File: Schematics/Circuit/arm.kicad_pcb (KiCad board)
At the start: 2 copper layers, 15.1 x 13.2 mm, 6 parts, among them IC1 VL53L0X, J1 Conn_01x07

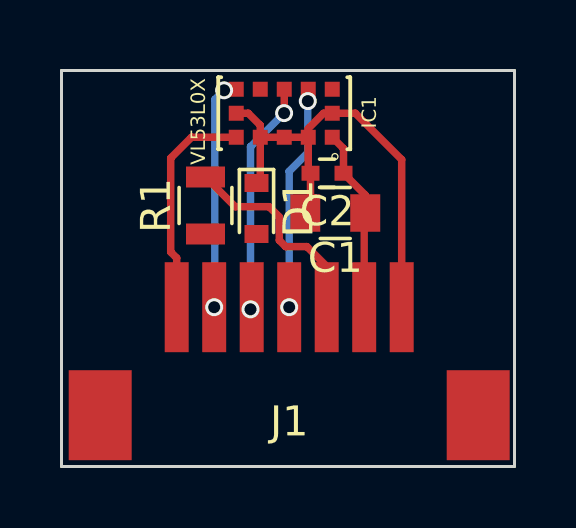
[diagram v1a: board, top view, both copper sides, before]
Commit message: Edit schematic and model, add images
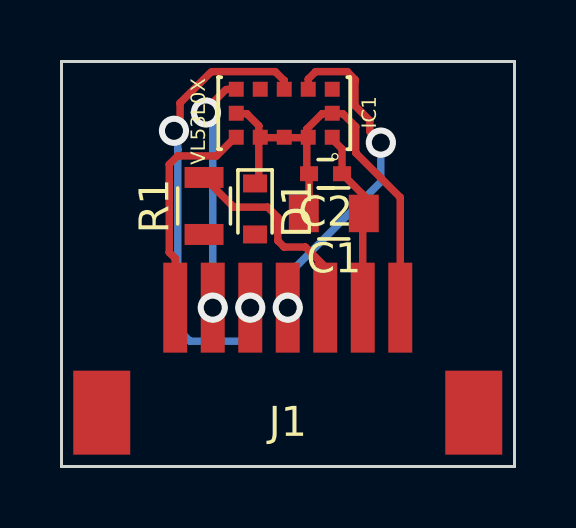
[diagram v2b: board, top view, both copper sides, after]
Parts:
- moved R1 0.05 mm to (19.1, 18.8)
- moved D1 0.05 mm to (20.8, 18.9)
- moved C1 0.05 mm to (23.4, 19.1)
- moved C2 0.05 mm to (23.1, 17.7)
- moved J1 0.05 mm to (21.8, 24.7)
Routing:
- net /SDA: track 7.89 -> 15.8 mm
- net /SCL: track 7.66 -> 11.5 mm
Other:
- board size 15.1 x 13.2 mm -> 15.1 x 13.5 mm
- net class Default: via_dia 0.6 -> 1.006; via_drill 0.4 -> 0.6
- rule trace_min: 0.2 -> 0.203
- rule via_min_drill: 0.3 -> 0.6
- rule via_min_size: 0.4 -> 1.006

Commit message: Add UV and Gamma detection, fix main pcb
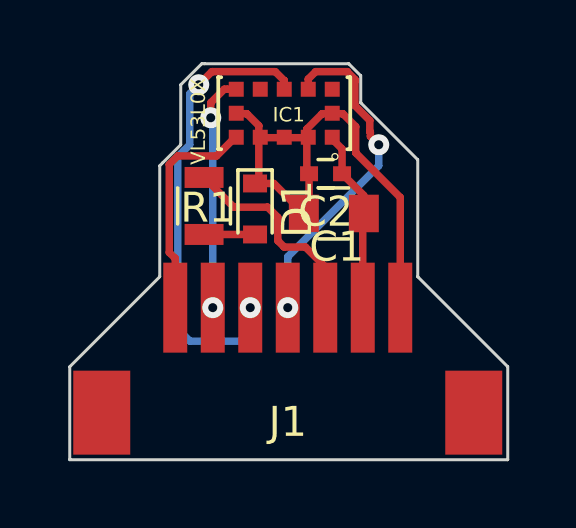
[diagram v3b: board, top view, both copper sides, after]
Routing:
- net GND: track 16.1 -> 18.2 mm
- net Net-(D1-Pad2): track 0.00 -> 1.70 mm
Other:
- board size 15.1 x 13.5 mm -> 14.6 x 13.2 mm
- net class Default: via_dia 1.006 -> 0.7; via_drill 0.6 -> 0.3
- rule via_min_drill: 0.6 -> 0.3
- rule via_min_size: 1.006 -> 0.7
